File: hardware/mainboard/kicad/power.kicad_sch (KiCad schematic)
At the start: 42 parts, among them J1 1S LiPo + NTC, SW1 HARD POWER, U2 TPS2121, U3 BQ25185DLHR, U4 TPS63802DLAR

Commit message: R32: add real JST PH SMT battery header including two mechanical anchors
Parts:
- J1: footprint Connector_Generic:JST_PH_3_PLACEMENT -> ENKU:JST_PH_S3B-PH-SM4-TB_1x03-1MP_P2.00mm_Horizontal
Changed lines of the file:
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@@
 		(property "Reference" "J1" (at 128.255 109.73 0) (effects (font (size 0.95 0.95))))
 		(property "Value" "1S LiPo + NTC" (at 142.255 109.73 0) (effects (font (size 0.95 0.95))))
-		(property "Footprint" "Connector_Generic:JST_PH_3_PLACEMENT" (at 135.255 125.73 0) (effects (font (size 0.95 0.95)) (hide yes)))
+		(property "Footprint" "ENKU:JST_PH_S3B-PH-SM4-TB_1x03-1MP_P2.00mm_Horizontal" (at 135.255 125.73 0) (effects (font (size 0.95 0.95)) (hide yes)))
 		(property "Datasheet" "~" (at 135.255 125.73 0) (effects (font (size 0.95 0.95)) (hide yes)))
 		(property "Description" "1S LiPo + NTC" (at 135.255 125.73 0) (effects (font (size 0.95 0.95)) (hide yes)))

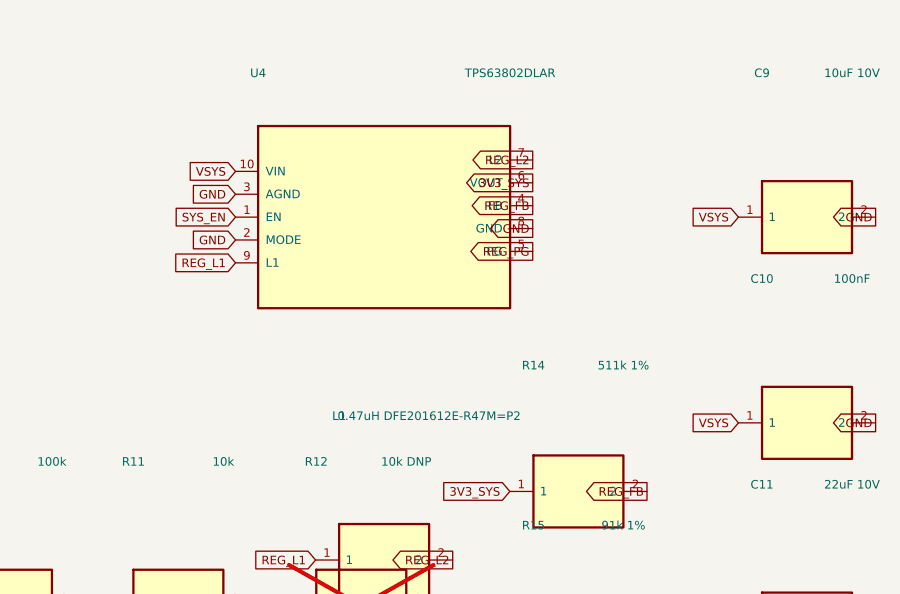
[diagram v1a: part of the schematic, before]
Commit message: R33: switch 3V3 converter VIN + EN + input capacitors downstream of mechanical SW1
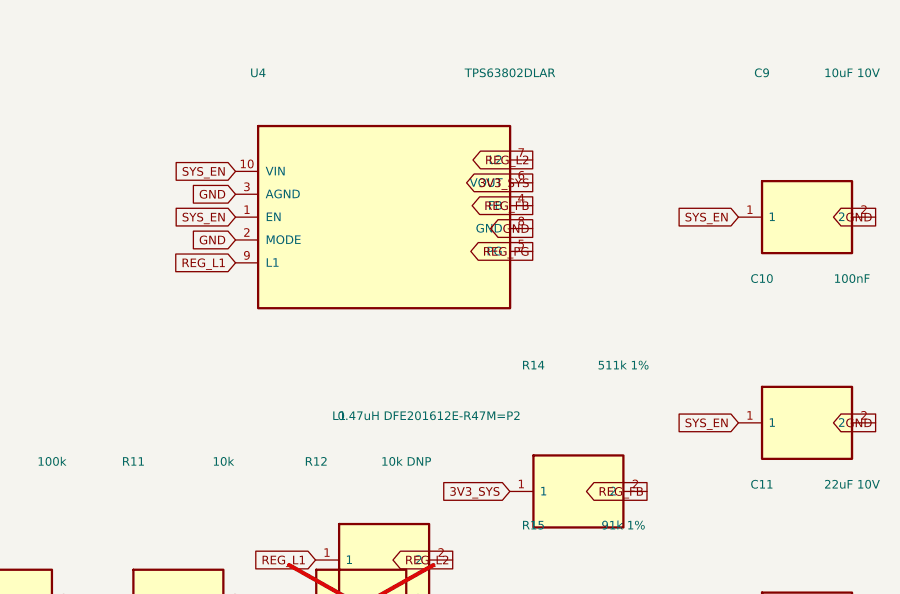
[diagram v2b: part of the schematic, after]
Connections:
- net SYS_EN: now also C10.1, C9.1, U4.10 (VIN)
- net VSYS: no longer C10.1, C9.1, U4.10 (VIN)
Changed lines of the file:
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@@
 	(global_label "REG_PG" (shape output) (at 220.98 66.04 180) (effects (font (size 0.95 0.95)) (justify right bottom)))
 	(global_label "REG_L1" (shape input) (at 187.96 67.31 0) (effects (font (size 0.95 0.95)) (justify right bottom)))
-	(global_label "VSYS" (shape input) (at 187.96 57.15 0) (effects (font (size 0.95 0.95)) (justify right bottom)))
+	(global_label "SYS_EN" (shape input) (at 187.96 57.15 0) (effects (font (size 0.95 0.95)) (justify right bottom)))
 	(global_label "SYS_EN" (shape input) (at 187.96 62.23 0) (effects (font (size 0.95 0.95)) (justify right bottom)))
 	(global_label "GND" (shape input) (at 187.96 64.77 0) (effects (font (size 0.95 0.95)) (justify right bottom)))
@@
 		(instances (project "enku-mainboard-r0.1" (path "/10000000-0000-4000-8000-000000000001/70000000-0000-4000-8000-000000000194" (reference "C9") (unit 1))))
 	)
-	(global_label "VSYS" (shape input) (at 243.84 62.23 0) (effects (font (size 0.95 0.95)) (justify right bottom)))
+	(global_label "SYS_EN" (shape input) (at 243.84 62.23 0) (effects (font (size 0.95 0.95)) (justify right bottom)))
 	(global_label "GND" (shape output) (at 259.08 62.23 180) (effects (font (size 0.95 0.95)) (justify right bottom)))
 	(symbol (lib_id "ENKU:C") (at 251.46 85.09 0) (unit 1) (exclude_from_sim no) (in_bom yes) (on_board yes) (dnp no)
@@
 		(instances (project "enku-mainboard-r0.1" (path "/10000000-0000-4000-8000-000000000001/70000000-0000-4000-8000-000000000199" (reference "C10") (unit 1))))
 	)
-	(global_label "VSYS" (shape input) (at 243.84 85.09 0) (effects (font (size 0.95 0.95)) (justify right bottom)))
+	(global_label "SYS_EN" (shape input) (at 243.84 85.09 0) (effects (font (size 0.95 0.95)) (justify right bottom)))
 	(global_label "GND" (shape output) (at 259.08 85.09 180) (effects (font (size 0.95 0.95)) (justify right bottom)))
 	(symbol (lib_id "ENKU:C") (at 251.46 107.95 0) (unit 1) (exclude_from_sim no) (in_bom yes) (on_board yes) (dnp no)

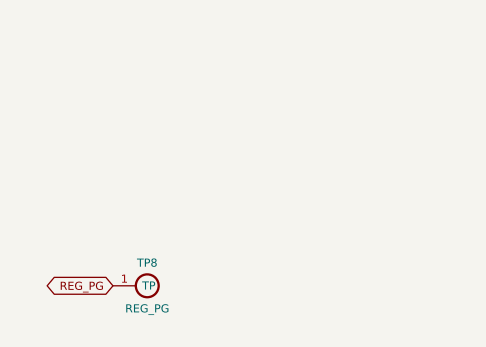
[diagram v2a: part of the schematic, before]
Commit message: R34: physically justified ERC power source flags on switched SYS_EN and pack GND
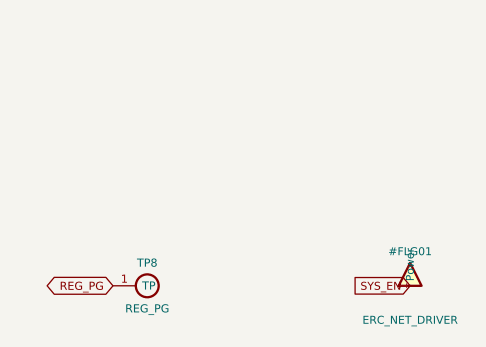
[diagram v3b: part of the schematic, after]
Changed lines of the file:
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@@
 )
 	(sheet_instances (path "/" (page "2")))
+	(symbol (lib_id "ENKU:ERC_NET_DRIVER") (at 274.32 180.34 0) (unit 1) (exclude_from_sim no) (in_bom no) (on_board no) (dnp no)
+  (property "Reference" "#FLG01" (at 274.32 176.53 0) (effects (font (size 0.88 0.88))))
+  (property "Value" "ERC_NET_DRIVER" (at 274.32 184.15 0) (effects (font (size 0.88 0.88))))
+  (property "Footprint" "" (at 274.32 180.34 0) (effects (font (size 0.88 0.88)) (hide yes)))
+  (property "Datasheet" "~" (at 274.32 180.34 0) (effects (font (size 0.88 0.88)) (hide yes)))
+  (pin "1")
+  (instances (project "enku-mainboard-r0.1" (path "/10000000-0000-4000-8000-000000000001/e4200000-0000-4000-8000-000000000010" (reference "#FLG01") (unit 1))))
 )
+(global_label "SYS_EN" (shape input) (at 274.32 180.34 0) (effects (font (size 0.88 0.88)) (justify right bottom)))
+)

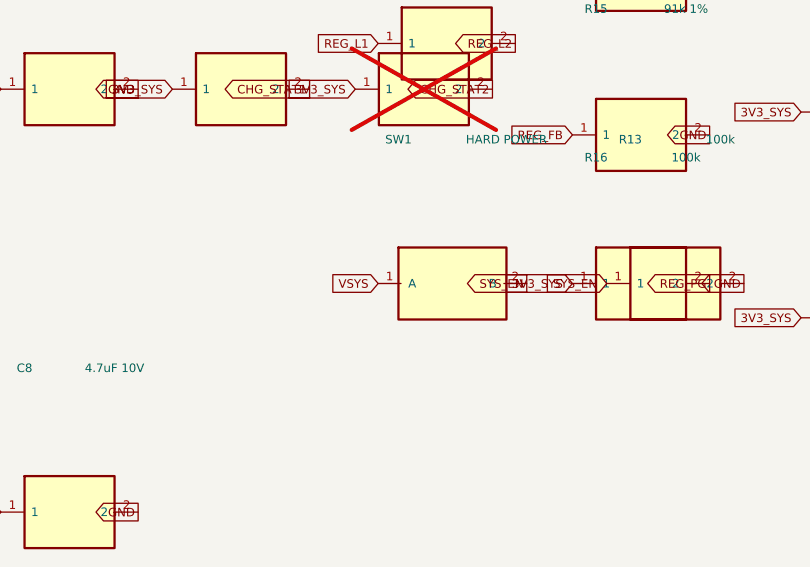
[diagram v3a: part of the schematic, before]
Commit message: R35: define embedded PMOS load switch and change front slider to gate-to-ground only
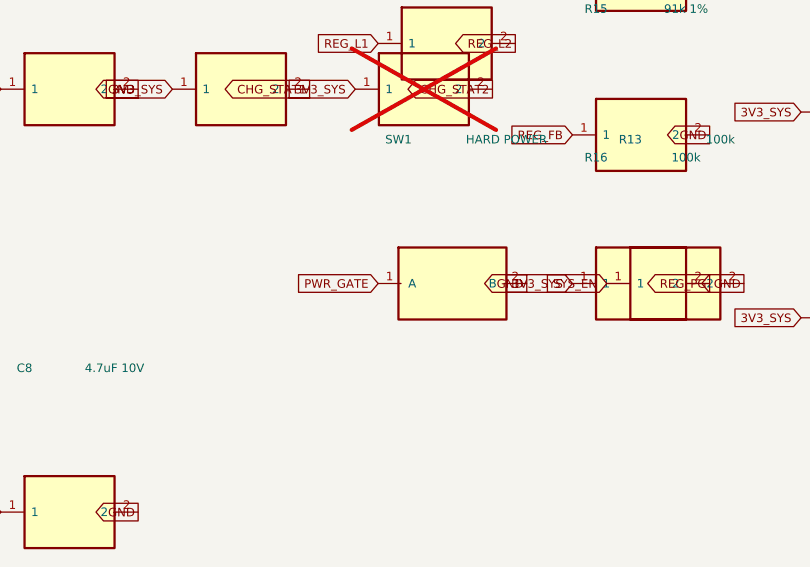
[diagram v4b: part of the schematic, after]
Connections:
- net GND: now also SW1.2 (B)
- net SYS_EN: no longer SW1.2 (B)
- net VSYS: no longer SW1.1 (A)
- new net PWR_GATE: SW1.1 (A)
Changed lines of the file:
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@@
 		(instances (project "enku-mainboard-r0.1" (path "/10000000-0000-4000-8000-000000000001/70000000-0000-4000-8000-000000000179" (reference "SW1") (unit 1))))
 	)
-	(global_label "VSYS" (shape input) (at 196.85 127 0) (effects (font (size 0.95 0.95)) (justify right bottom)))
-	(global_label "SYS_EN" (shape output) (at 213.36 127 180) (effects (font (size 0.95 0.95)) (justify right bottom)))
+	(global_label "PWR_GATE" (shape input) (at 196.85 127 0) (effects (font (size 0.95 0.95)) (justify right bottom)))
+	(global_label "GND" (shape output) (at 213.36 127 180) (effects (font (size 0.95 0.95)) (justify right bottom)))
 	(symbol (lib_id "ENKU:R") (at 229.87 127 0) (unit 1) (exclude_from_sim no) (in_bom yes) (on_board yes) (dnp no)
 		(property "Reference" "R13" (at 224.87 111 0) (effects (font (size 0.95 0.95))))

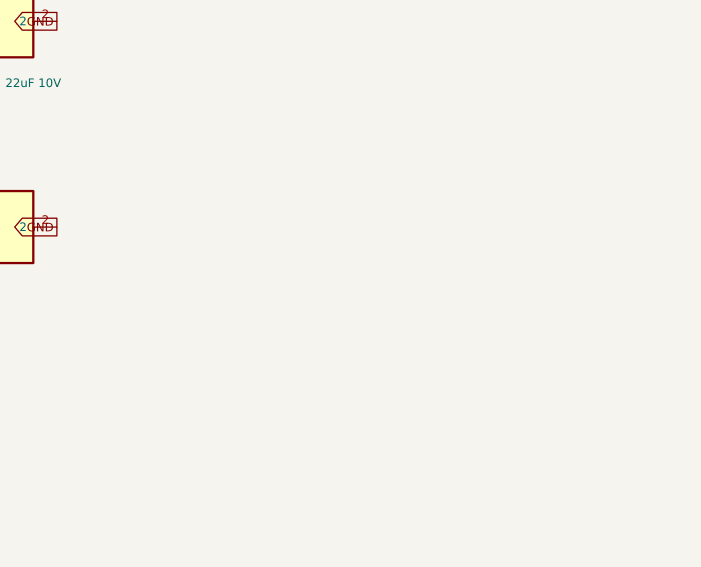
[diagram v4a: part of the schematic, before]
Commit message: R35: wire AO3401A source VSYS/drain SYS_EN/gate PWR_GATE plus local pull-up R40 in KiCad schematic
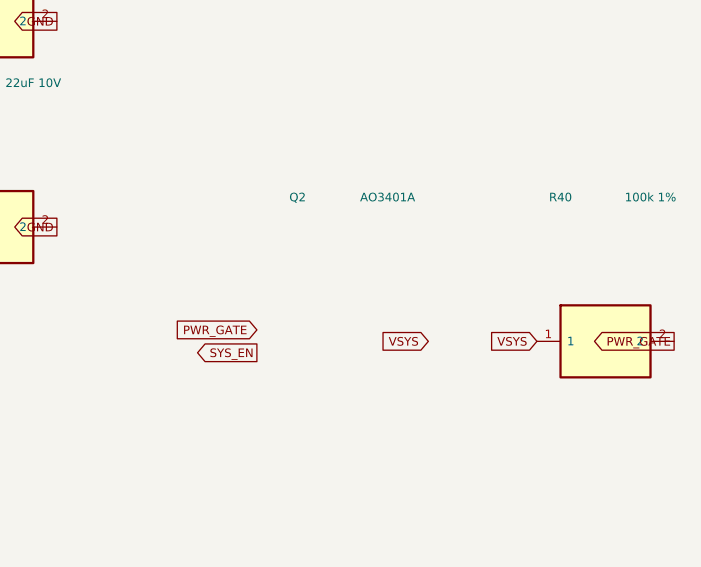
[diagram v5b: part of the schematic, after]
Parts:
- added Q2: AO3401A, Package_TO_SOT_SMD:SOT-23, symbol ENKU:PMOS_LOAD
- added R40: 100k 1%, Resistor_SMD:R_0603_1608Metric, symbol ENKU:R
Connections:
- net PWR_GATE: now also R40.2
- net VSYS: now also R40.1
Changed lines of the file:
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@@
 )
 (global_label "SYS_EN" (shape input) (at 274.32 180.34 0) (effects (font (size 0.88 0.88)) (justify right bottom)))
+	(symbol (lib_id "ENKU:PMOS_LOAD") (at 290.83 143.51 0) (unit 1) (exclude_from_sim no) (in_bom yes) (on_board yes) (dnp no)
+ (property "Reference" "Q2" (at 285.83 127.50999999999999 0) (effects (font (size 0.95 0.95))))
+ (property "Value" "AO3401A" (at 295.83 127.50999999999999 0) (effects (font (size 0.95 0.95))))
+ (property "Footprint" "Package_TO_SOT_SMD:SOT-23" (at 290.83 143.51 0) (effects (font (size 0.95 0.95)) (hide yes)))
+ (property "Datasheet" "https://www.aosmd.com/sites/default/files/res/data_sheets/AO3401A.pdf" (at 290.83 143.51 0) (effects (font (size 0.95 0.95)) (hide yes)))
+ (property "Description" "AO3401A" (at 290.83 143.51 0) (effects (font (size 0.95 0.95)) (hide yes)))
+ (pin "1")
+ (pin "3")
+ (pin "2")
+ (instances (project "enku-mainboard-r0.1" (path "/10000000-0000-4000-8000-000000000001/e5100000-0000-4000-8000-000000000001" (reference "Q2") (unit 1))))
 )
+	(symbol (lib_id "ENKU:R") (at 320.04 143.51 0) (unit 1) (exclude_from_sim no) (in_bom yes) (on_board yes) (dnp no)
+ (property "Reference" "R40" (at 315.04 127.50999999999999 0) (effects (font (size 0.95 0.95))))
+ (property "Value" "100k 1%" (at 325.04 127.50999999999999 0) (effects (font (size 0.95 0.95))))
+ (property "Footprint" "Resistor_SMD:R_0603_1608Metric" (at 320.04 143.51 0) (effects (font (size 0.95 0.95)) (hide yes)))
+ (property "Datasheet" "~" (at 320.04 143.51 0) (effects (font (size 0.95 0.95)) (hide yes)))
+ (property "Description" "100k 1%" (at 320.04 143.51 0) (effects (font (size 0.95 0.95)) (hide yes)))
+ (pin "1")
+ (pin "2")
+ (instances (project "enku-mainboard-r0.1" (path "/10000000-0000-4000-8000-000000000001/e5100000-0000-4000-8000-000000000015" (reference "R40") (unit 1))))
+)
+	(global_label "PWR_GATE" (shape input) (at 281.305 142.24 0) (effects (font (size 0.95 0.95)) (justify right bottom)))
+	(global_label "SYS_EN" (shape output) (at 281.305 144.78 0) (effects (font (size 0.95 0.95)) (justify right bottom)))
+	(global_label "VSYS" (shape input) (at 300.355 143.51 180) (effects (font (size 0.95 0.95)) (justify right bottom)))
+	(global_label "VSYS" (shape input) (at 312.42 143.51 0) (effects (font (size 0.95 0.95)) (justify right bottom)))
+	(global_label "PWR_GATE" (shape output) (at 327.66 143.51 180) (effects (font (size 0.95 0.95)) (justify right bottom)))
+)

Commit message: R35: repair premature PMOS symbol S-expression closure and restore full embedded 3-pin definition
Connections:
- net PWR_GATE: now also Q2.1 (G)
- net SYS_EN: now also Q2.3 (D)
- net VSYS: now also Q2.2 (S)

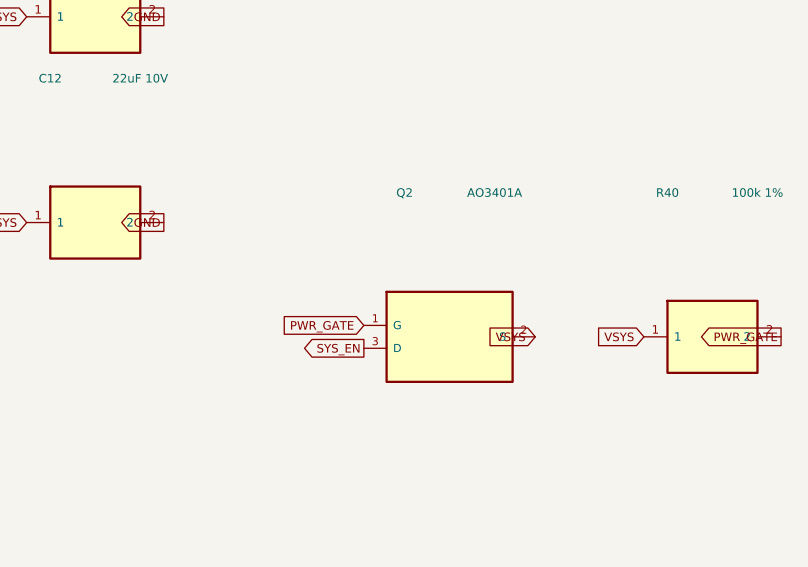
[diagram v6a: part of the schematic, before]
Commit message: R35: align Q2 gate/drain/source schematic pins to KiCad 1.27mm ERC grid
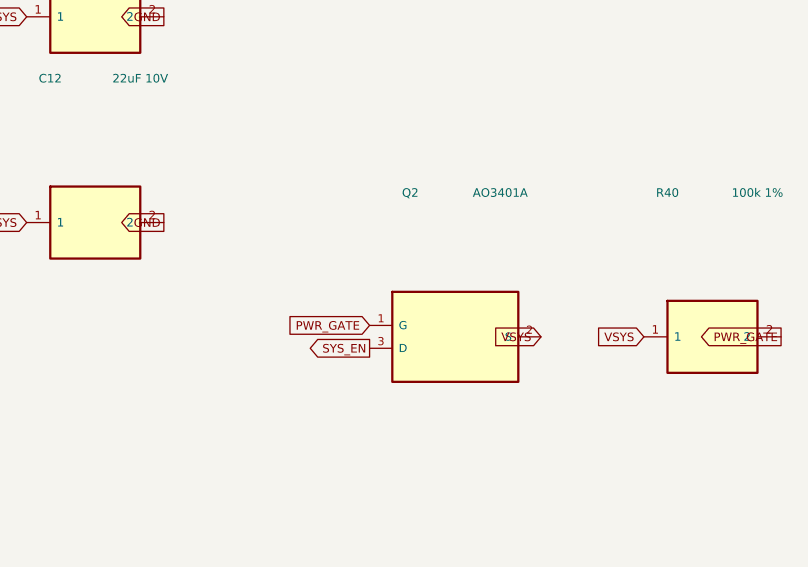
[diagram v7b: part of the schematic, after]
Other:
- moved on the sheet: Q2
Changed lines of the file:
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@@
 )
 (global_label "SYS_EN" (shape input) (at 274.32 180.34 0) (effects (font (size 0.88 0.88)) (justify right bottom)))
-	(symbol (lib_id "ENKU:PMOS_LOAD") (at 290.83 143.51 0) (unit 1) (exclude_from_sim no) (in_bom yes) (on_board yes) (dnp no)
- (property "Reference" "Q2" (at 285.83 127.50999999999999 0) (effects (font (size 0.95 0.95))))
- (property "Value" "AO3401A" (at 295.83 127.50999999999999 0) (effects (font (size 0.95 0.95))))
- (property "Footprint" "Package_TO_SOT_SMD:SOT-23" (at 290.83 143.51 0) (effects (font (size 0.95 0.95)) (hide yes)))
- (property "Datasheet" "https://www.aosmd.com/sites/default/files/res/data_sheets/AO3401A.pdf" (at 290.83 143.51 0) (effects (font (size 0.95 0.95)) (hide yes)))
- (property "Description" "AO3401A" (at 290.83 143.51 0) (effects (font (size 0.95 0.95)) (hide yes)))
+	(symbol (lib_id "ENKU:PMOS_LOAD") (at 291.465 143.51 0) (unit 1) (exclude_from_sim no) (in_bom yes) (on_board yes) (dnp no)
+ (property "Reference" "Q2" (at 286.465 127.50999999999999 0) (effects (font (size 0.95 0.95))))
+ (property "Value" "AO3401A" (at 296.465 127.50999999999999 0) (effects (font (size 0.95 0.95))))
+ (property "Footprint" "Package_TO_SOT_SMD:SOT-23" (at 291.465 143.51 0) (effects (font (size 0.95 0.95)) (hide yes)))
+ (property "Datasheet" "https://www.aosmd.com/sites/default/files/res/data_sheets/AO3401A.pdf" (at 291.465 143.51 0) (effects (font (size 0.95 0.95)) (hide yes)))
+ (property "Description" "AO3401A" (at 291.465 143.51 0) (effects (font (size 0.95 0.95)) (hide yes)))
  (pin "1")
  (pin "3")
@@
  (instances (project "enku-mainboard-r0.1" (path "/10000000-0000-4000-8000-000000000001/e5100000-0000-4000-8000-000000000015" (reference "R40") (unit 1))))
 )
-	(global_label "PWR_GATE" (shape input) (at 281.305 142.24 0) (effects (font (size 0.95 0.95)) (justify right bottom)))
-	(global_label "SYS_EN" (shape output) (at 281.305 144.78 0) (effects (font (size 0.95 0.95)) (justify right bottom)))
-	(global_label "VSYS" (shape input) (at 300.355 143.51 180) (effects (font (size 0.95 0.95)) (justify right bottom)))
+	(global_label "PWR_GATE" (shape input) (at 281.94 142.24 0) (effects (font (size 0.95 0.95)) (justify right bottom)))
+	(global_label "SYS_EN" (shape output) (at 281.94 144.78 0) (effects (font (size 0.95 0.95)) (justify right bottom)))
+	(global_label "VSYS" (shape input) (at 300.99 143.51 180) (effects (font (size 0.95 0.95)) (justify right bottom)))
 	(global_label "VSYS" (shape input) (at 312.42 143.51 0) (effects (font (size 0.95 0.95)) (justify right bottom)))
 	(global_label "PWR_GATE" (shape output) (at 327.66 143.51 180) (effects (font (size 0.95 0.95)) (justify right bottom)))

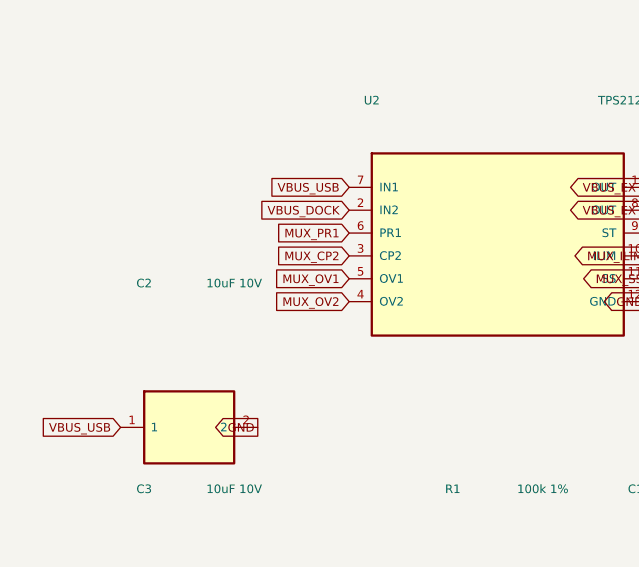
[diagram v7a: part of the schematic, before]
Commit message: R41: implement switched-rail fail-safe VBUS comparator, discharge model, SD supply and dual ground references
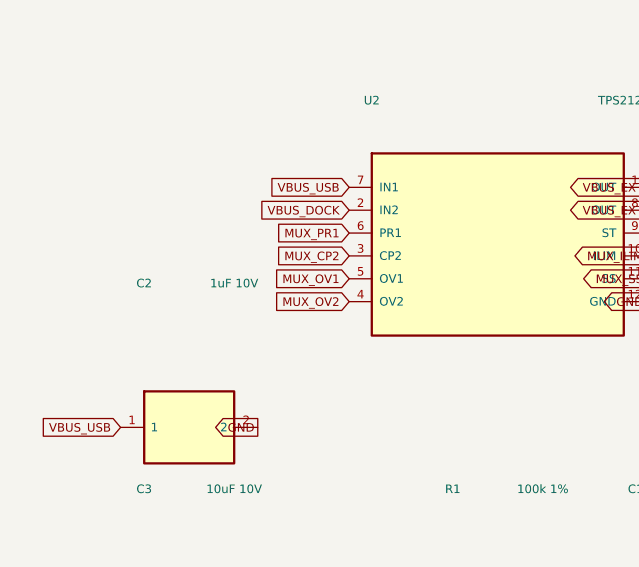
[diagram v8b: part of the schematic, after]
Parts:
- C2: value 10uF 10V -> 1uF 10V
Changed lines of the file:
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@@
 	(symbol (lib_id "ENKU:C") (at 27.94 82.55 0) (unit 1) (exclude_from_sim no) (in_bom yes) (on_board yes) (dnp no)
 		(property "Reference" "C2" (at 22.94 66.55 0) (effects (font (size 0.95 0.95))))
-		(property "Value" "10uF 10V" (at 32.94 66.55 0) (effects (font (size 0.95 0.95))))
+		(property "Value" "1uF 10V" (at 32.94 66.55 0) (effects (font (size 0.95 0.95))))
 		(property "Footprint" "Capacitor_SMD:C_0805_2012Metric" (at 27.94 82.55 0) (effects (font (size 0.95 0.95)) (hide yes)))
 		(property "Datasheet" "~" (at 27.94 82.55 0) (effects (font (size 0.95 0.95)) (hide yes)))
-		(property "Description" "10uF 10V" (at 27.94 82.55 0) (effects (font (size 0.95 0.95)) (hide yes)))
+		(property "Description" "1uF 10V" (at 27.94 82.55 0) (effects (font (size 0.95 0.95)) (hide yes)))
 		(pin "1")
 		(pin "2")
